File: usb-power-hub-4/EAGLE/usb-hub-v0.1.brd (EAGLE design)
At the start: 90 x 25 mm, 37 parts, among them U1 RICHTEKRT9715AGBR, U2 RICHTEKRT9715AGBR, U3 RICHTEKRT9715AGBR, U4 RICHTEKRT9715AGBR

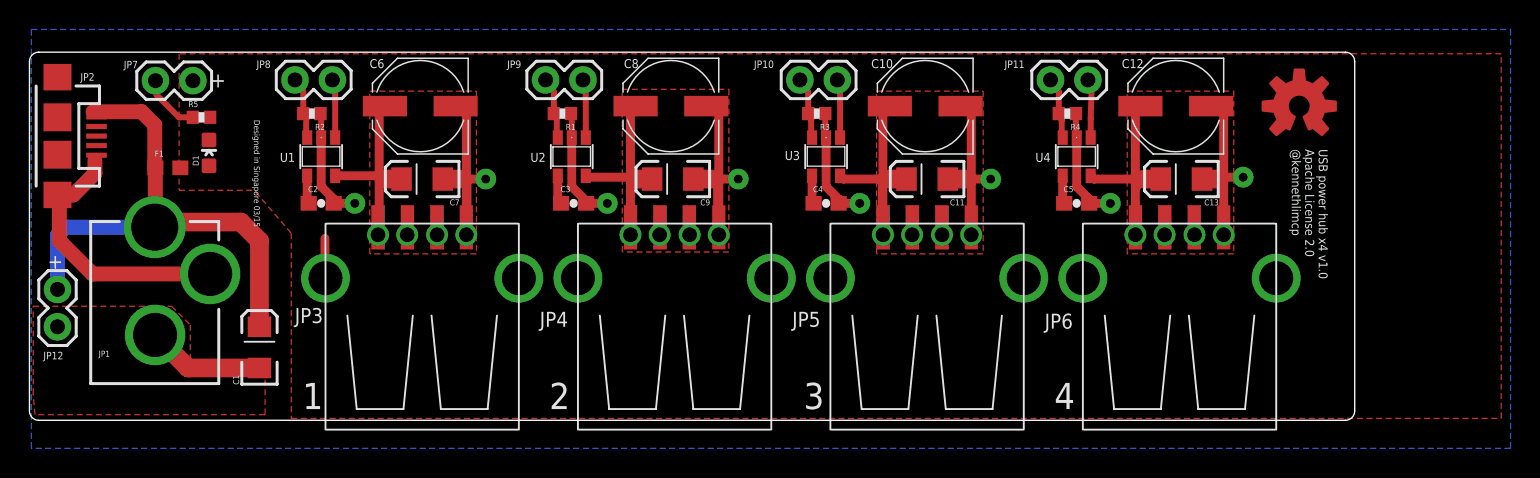
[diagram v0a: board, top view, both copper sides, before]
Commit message: Fixed top silkscreen
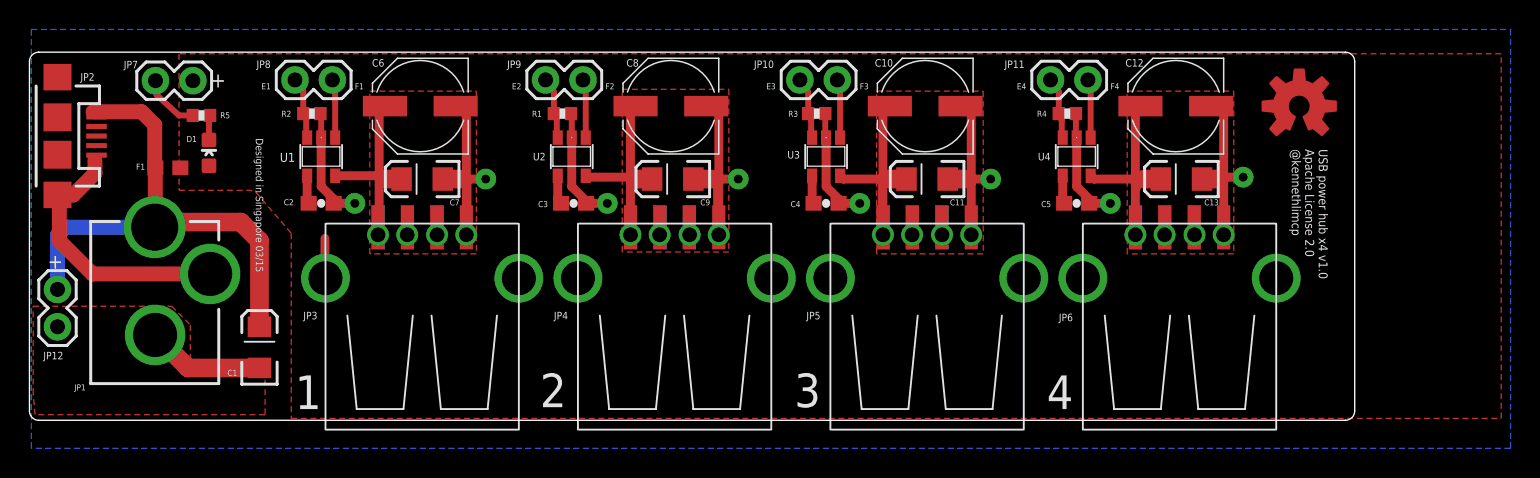
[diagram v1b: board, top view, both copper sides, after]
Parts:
- moved R5 0.13 mm to (11.7, 20.7)
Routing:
- net N$5: track 0.00 -> 1.68 mm
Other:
- board text added: "E1"
- board text added: "E2"
- board text added: "E3"
- board text added: "E4"
- board text added: "F1"
- board text added: "F2"
- board text added: "F3"
- board text added: "F4"
